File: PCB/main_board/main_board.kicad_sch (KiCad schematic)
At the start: 55 parts, among them CN1 XT30PW-M, CN2 XT30PW-M, U1 XT30PW-F, U2 W25Q32JVUUIQ, U3 W25N01GVZEIG_C907680, U4 INA226, U5 INA226, U6 RP2040, U7 AZ1117-3.3, X1 X322512MSB4SI

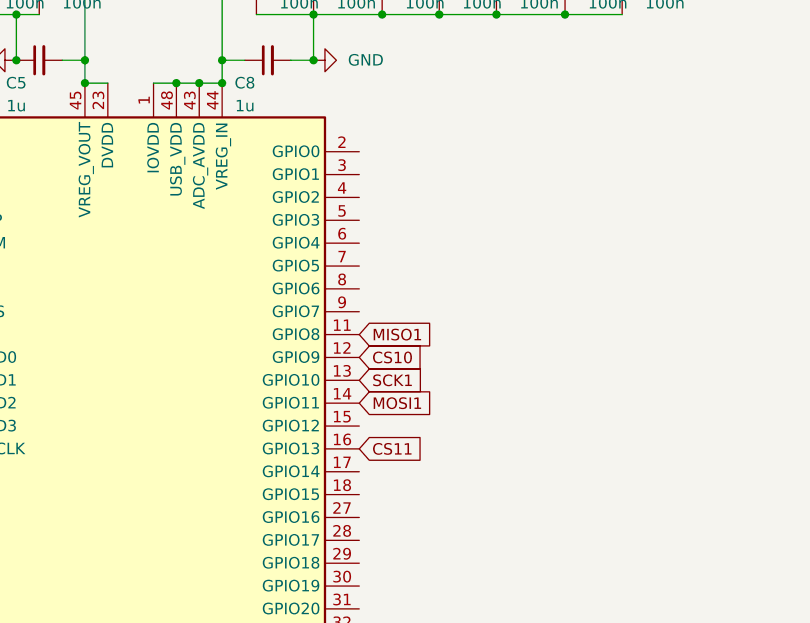
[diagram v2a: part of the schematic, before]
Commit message: Change IIC0, IIC1 and SPI connection GPIO
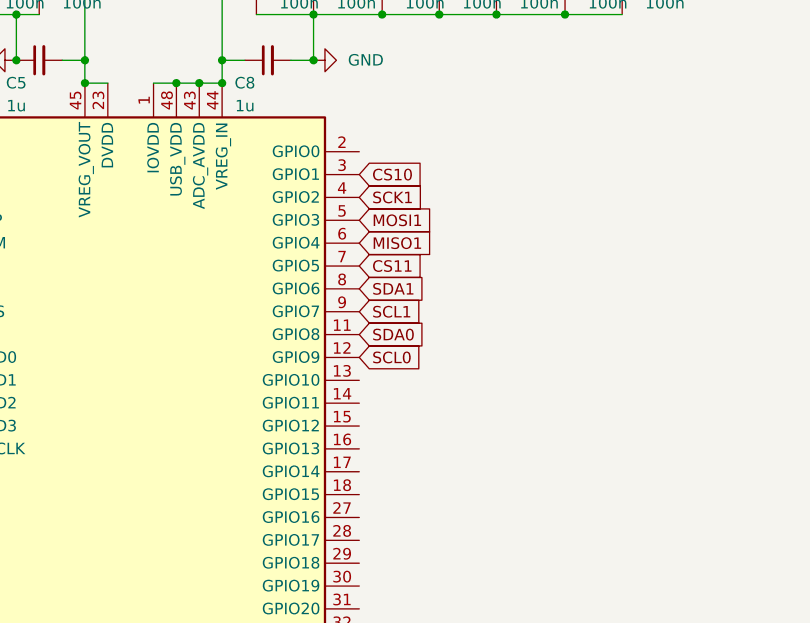
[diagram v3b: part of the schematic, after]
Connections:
- net CS10: now also U6.3 (GPIO1); no longer U6.12 (GPIO9)
- net CS11: now also U6.7 (GPIO5); no longer U6.16 (GPIO13)
- net MISO1: now also U6.6 (GPIO4); no longer U6.11 (GPIO8)
- net MOSI1: now also U6.5 (GPIO3); no longer U6.14 (GPIO11)
- net SCK1: now also U6.4 (GPIO2); no longer U6.13 (GPIO10)
- net SCL0: now also U6.12 (GPIO9)
- net SCL1: now also U6.9 (GPIO7)
- net SDA0: now also U6.11 (GPIO8)
- net SDA1: now also U6.8 (GPIO6)
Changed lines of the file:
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@@
     )
   )
-  (global_label "SCK1" (shape input) (at 138.43 196.85 0) (fields_autoplaced)
-    (effects (font (size 1.27 1.27)) (justify left))
-    (property "Intersheetrefs" "${INTERSHEET_REFS}" (at 146.2948 196.85 0)
+  (global_label "CS10" (shape input) (at 138.43 173.99 0) (fields_autoplaced)
+    (effects (font (size 1.27 1.27)) (justify left))
+    (property "Intersheetrefs" "${INTERSHEET_REFS}" (at 146.2343 173.99 0)
+      (effects (font (size 1.27 1.27)) (justify left) hide)
+    )
+  )
+  (global_label "MISO1" (shape input) (at 138.43 181.61 0) (fields_autoplaced)
+    (effects (font (size 1.27 1.27)) (justify left))
+    (property "Intersheetrefs" "${INTERSHEET_REFS}" (at 147.1415 181.61 0)
+      (effects (font (size 1.27 1.27)) (justify left) hide)
+    )
+  )
+  (global_label "SCK1" (shape input) (at 138.43 176.53 0) (fields_autoplaced)
+    (effects (font (size 1.27 1.27)) (justify left))
+    (property "Intersheetrefs" "${INTERSHEET_REFS}" (at 146.2948 176.53 0)
       (effects (font (size 1.27 1.27)) (justify left) hide)
     )
@@
     )
   )
-  (global_label "MISO1" (shape input) (at 138.43 191.77 0) (fields_autoplaced)
-    (effects (font (size 1.27 1.27)) (justify left))
-    (property "Intersheetrefs" "${INTERSHEET_REFS}" (at 147.1415 191.77 0)
-      (effects (font (size 1.27 1.27)) (justify left) hide)
-    )
-  )
   (global_label "IBAT-" (shape input) (at 46.99 110.49 180) (fields_autoplaced)
     (effects (font (size 1.27 1.27)) (justify right))
@@
     )
   )
-  (global_label "CS11" (shape input) (at 138.43 204.47 0) (fields_autoplaced)
-    (effects (font (size 1.27 1.27)) (justify left))
-    (property "Intersheetrefs" "${INTERSHEET_REFS}" (at 146.2343 204.47 0)
+  (global_label "SCL1" (shape input) (at 138.43 189.23 0) (fields_autoplaced)
+    (effects (font (size 1.27 1.27)) (justify left))
+    (property "Intersheetrefs" "${INTERSHEET_REFS}" (at 146.0529 189.23 0)
       (effects (font (size 1.27 1.27)) (justify left) hide)
     )
@@
     )
   )
+  (global_label "CS11" (shape input) (at 138.43 184.15 0) (fields_autoplaced)
+    (effects (font (size 1.27 1.27)) (justify left))
+    (property "Intersheetrefs" "${INTERSHEET_REFS}" (at 146.2343 184.15 0)
+      (effects (font (size 1.27 1.27)) (justify left) hide)
+    )
+  )
   (global_label "CS11" (shape input) (at 213.36 207.01 180) (fields_autoplaced)
     (effects (font (size 1.27 1.27)) (justify right))
@@
     )
   )
+  (global_label "MOSI1" (shape input) (at 138.43 179.07 0) (fields_autoplaced)
+    (effects (font (size 1.27 1.27)) (justify left))
+    (property "Intersheetrefs" "${INTERSHEET_REFS}" (at 147.1415 179.07 0)
+      (effects (font (size 1.27 1.27)) (justify left) hide)
+    )
+  )
   (global_label "SDA1" (shape input) (at 168.91 110.49 270) (fields_autoplaced)
     (effects (font (size 1.27 1.27)) (justify right))
@@
     )
   )
+  (global_label "SCL0" (shape input) (at 138.43 194.31 0) (fields_autoplaced)
+    (effects (font (size 1.27 1.27)) (justify left))
+    (property "Intersheetrefs" "${INTERSHEET_REFS}" (at 146.0529 194.31 0)
+      (effects (font (size 1.27 1.27)) (justify left) hide)
+    )
+  )
   (global_label "SD2" (shape input) (at 210.82 245.11 180) (fields_autoplaced)
     (effects (font (size 1.27 1.27)) (justify right))
@@
     )
   )
+  (global_label "SDA1" (shape input) (at 138.43 186.69 0) (fields_autoplaced)
+    (effects (font (size 1.27 1.27)) (justify left))
+    (property "Intersheetrefs" "${INTERSHEET_REFS}" (at 146.1134 186.69 0)
+      (effects (font (size 1.27 1.27)) (justify left) hide)
+    )
+  )
   (global_label "SCK1" (shape input) (at 218.44 182.88 180) (fields_autoplaced)
     (effects (font (size 1.27 1.27)) (justify right))
@@
     )
   )
-  (global_label "MOSI1" (shape input) (at 138.43 199.39 0) (fields_autoplaced)
-    (effects (font (size 1.27 1.27)) (justify left))
-    (property "Intersheetrefs" "${INTERSHEET_REFS}" (at 147.1415 199.39 0)
-      (effects (font (size 1.27 1.27)) (justify left) hide)
-    )
-  )
   (global_label "SD1" (shape input) (at 87.63 196.85 180) (fields_autoplaced)
     (effects (font (size 1.27 1.27)) (justify right))
@@
     )
   )
+  (global_label "SDA0" (shape input) (at 138.43 191.77 0) (fields_autoplaced)
+    (effects (font (size 1.27 1.27)) (justify left))
+    (property "Intersheetrefs" "${INTERSHEET_REFS}" (at 146.1134 191.77 0)
+      (effects (font (size 1.27 1.27)) (justify left) hide)
+    )
+  )
   (global_label "MOSI1" (shape input) (at 218.44 177.8 180) (fields_autoplaced)
     (effects (font (size 1.27 1.27)) (justify right))
@@
     )
   )
-  (global_label "CS10" (shape input) (at 138.43 194.31 0) (fields_autoplaced)
-    (effects (font (size 1.27 1.27)) (justify left))
-    (property "Intersheetrefs" "${INTERSHEET_REFS}" (at 146.2343 194.31 0)
-      (effects (font (size 1.27 1.27)) (justify left) hide)
-    )
-  )

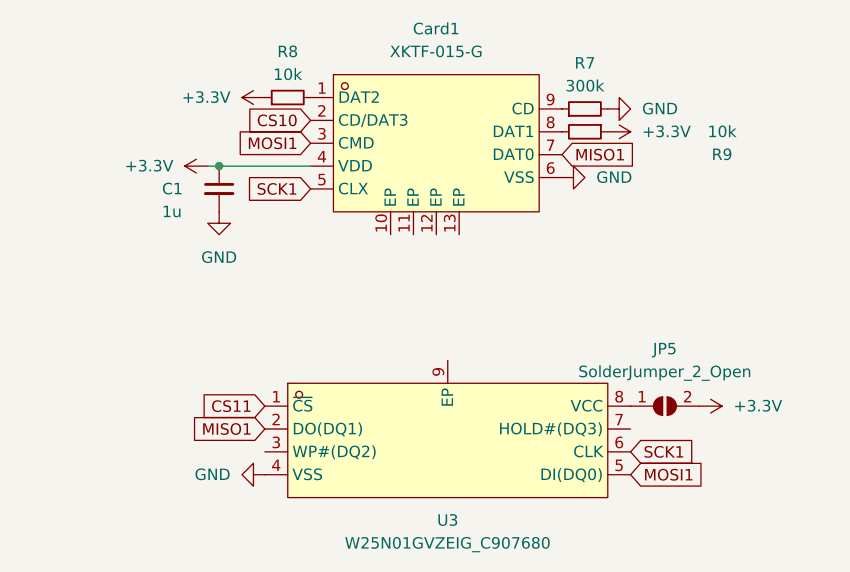
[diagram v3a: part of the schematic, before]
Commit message: Complete SPI Flash and part of decouple capacitor layout
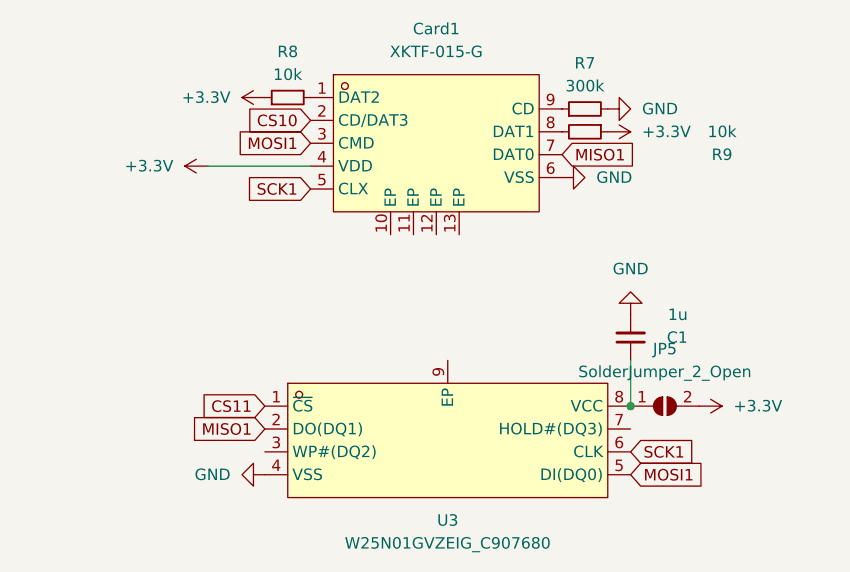
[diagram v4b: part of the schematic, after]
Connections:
- net +3.3V: no longer C1.1
- net at JP5.1 (A), U3.8 (VCC): now also C1.1
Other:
- moved on the sheet: C1
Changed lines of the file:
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@@
   (junction (at 102.87 151.13) (diameter 0) (color 0 0 0 0)
   )
-  (junction (at 208.28 180.34) (diameter 0) (color 0 0 0 0)
-  )
   (junction (at 133.35 151.13) (diameter 0) (color 0 0 0 0)
   )
@@
   (junction (at 127 151.13) (diameter 0) (color 0 0 0 0)
   )
+  (junction (at 254 207.01) (diameter 0) (color 0 0 0 0)
+  )
   (junction (at 133.35 161.29) (diameter 0) (color 0 0 0 0)
   )
@@
     (stroke (width 0) (type default))
   )
-  (wire (pts (xy 207.01 180.34) (xy 208.28 180.34))
-    (stroke (width 0) (type default))
-  )
   (wire (pts (xy 147.32 156.21) (xy 153.67 156.21))
     (stroke (width 0) (type default))
@@
     (stroke (width 0) (type default))
   )
-  (wire (pts (xy 208.28 180.34) (xy 218.44 180.34))
+  (wire (pts (xy 254 201.93) (xy 254 207.01))
+    (stroke (width 0) (type default))
+  )
+  (wire (pts (xy 207.01 180.34) (xy 218.44 180.34))
     (stroke (width 0) (type default))
   )
@@
     )
   )
-  (symbol (lib_id "power:GND") (at 208.28 185.42 0) (unit 1)
+  (symbol (lib_id "power:GND") (at 254 196.85 180) (unit 1)
     (in_bom yes) (on_board yes) (dnp no) (fields_autoplaced)
-    (property "Reference" "#PWR05" (at 208.28 191.77 0)
+    (property "Reference" "#PWR05" (at 254 190.5 0)
       (effects (font (size 1.27 1.27)) hide)
     )
-    (property "Value" "GND" (at 208.28 190.5 0)
+    (property "Value" "GND" (at 254 191.77 0)
       (effects (font (size 1.27 1.27)))
     )
-    (property "Footprint" "" (at 208.28 185.42 0)
+    (property "Footprint" "" (at 254 196.85 0)
       (effects (font (size 1.27 1.27)) hide)
     )
-    (property "Datasheet" "" (at 208.28 185.42 0)
+    (property "Datasheet" "" (at 254 196.85 0)
       (effects (font (size 1.27 1.27)) hide)
     )
@@
     )
   )
-  (symbol (lib_id "Device:C_Small") (at 208.28 182.88 0) (unit 1)
+  (symbol (lib_id "Device:C_Small") (at 254 199.39 180) (unit 1)
     (in_bom yes) (on_board yes) (dnp no)
-    (property "Reference" "C1" (at 201.93 182.88 0)
+    (property "Reference" "C1" (at 260.35 199.39 0)
       (effects (font (size 1.27 1.27)) (justify left))
     )
-    (property "Value" "1u" (at 201.93 185.42 0)
+    (property "Value" "1u" (at 260.35 196.85 0)
       (effects (font (size 1.27 1.27)) (justify left))
     )
-    (property "Footprint" "Capacitor_SMD:C_0402_1005Metric" (at 208.28 182.88 0)
+    (property "Footprint" "Capacitor_SMD:C_0402_1005Metric" (at 254 199.39 0)
       (effects (font (size 1.27 1.27)) hide)
     )
-    (property "Datasheet" "~" (at 208.28 182.88 0)
+    (property "Datasheet" "~" (at 254 199.39 0)
       (effects (font (size 1.27 1.27)) hide)
     )
